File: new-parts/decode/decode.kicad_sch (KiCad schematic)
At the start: 37 parts, among them J1 BHR-10-VUA, J10 Conn_02x01, J11 Conn_02x01, J12 Conn_02x01, J13 Conn_02x01, J14 Conn_02x01, J2 Conn_02x01, J3 Conn_02x01, J4 Conn_02x01, J5 Conn_02x01, J6 Conn_02x03_Odd_Even, J7 Conn_02x01, J8 Conn_02x01, J9 Conn_02x01, K1 J104D2C12VDC.15S, K2 J104D2C12VDC.15S, K3 J104D2C12VDC.15S, K4 J104D2C12VDC.15S, K5 J104D2C12VDC.15S, K6 J104D2C12VDC.15S, K7 J104D2C12VDC.15S, K8 J104D2C12VDC.15S, K9 J104D2C12VDC.15S

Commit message: Layout decoder.
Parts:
- added TP2, TP3, TP4, TP5, TP6, TP7, TP8: TestPoint, TestPoint:TestPoint_Pad_D1.5mm, symbol Connector:TestPoint
- renumbered K4 to K3, K3 to K4
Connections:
- net GND: now also K9.22; no longer K9.12
- net VCC: now also K9.24; no longer K9.14
- net a en: now also K1.24, TP6.1; no longer K1.14
- net a en out: now also J4.1 (Pin_1), K1.21; no longer J3.1 (Pin_1), K1.11
- net add: now also TP3.1
- net c2: now also TP4.1
- net cf: now also K9.21; no longer K9.11
- net cinv: now also TP5.1
- net cond: now also TP2.1
- net m en: now also TP8.1
- net p en: now also K1.14, TP7.1; no longer K1.24
- net p en out: now also J3.1 (Pin_1), K1.11; no longer J4.1 (Pin_1), K1.21
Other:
- note added: "operand source out"
- note removed: "result source out"
- moved on the sheet: J10, J11, J12, J13, J14, J2, J6, J7, J8, J9

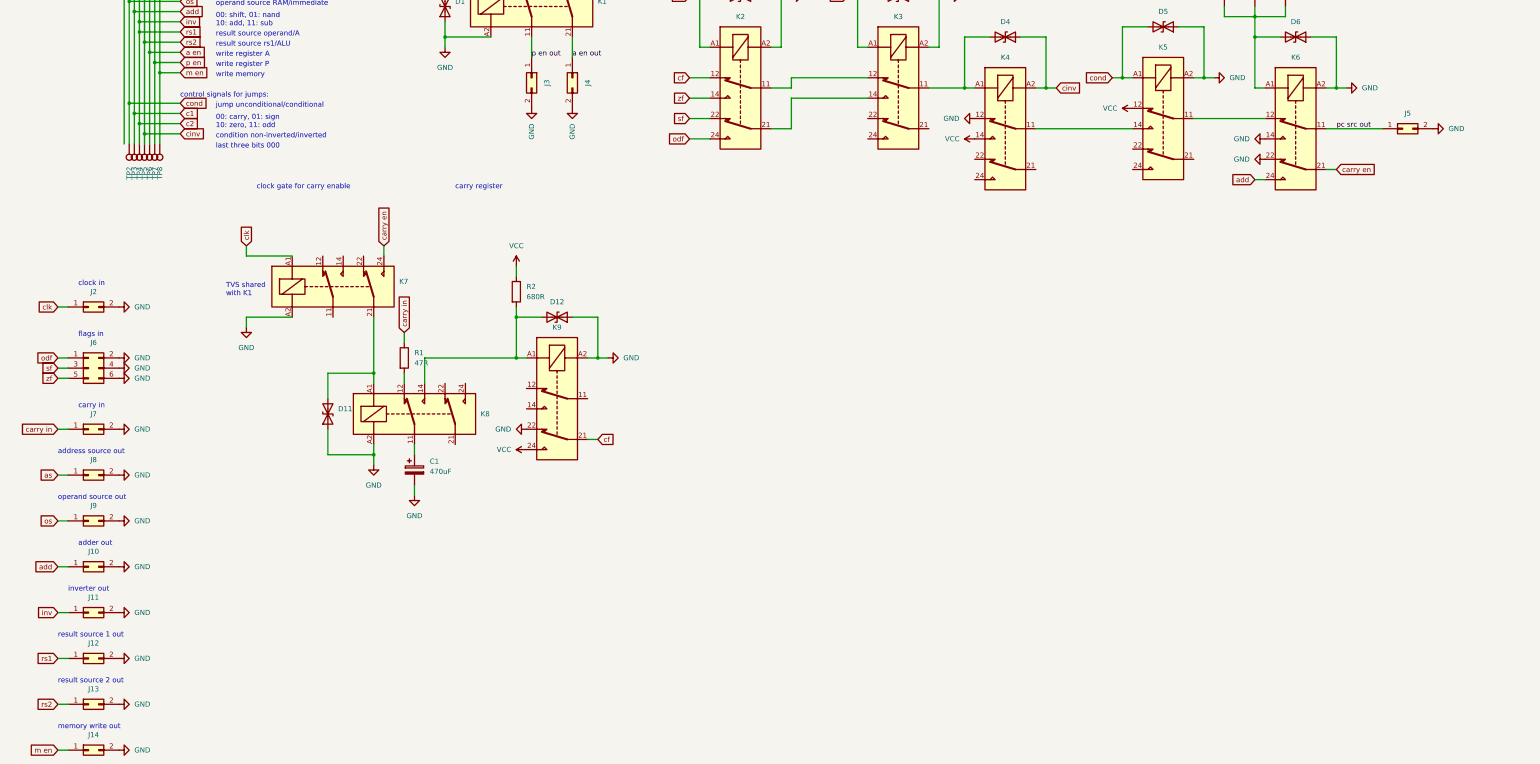
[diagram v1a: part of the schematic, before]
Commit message: Change all two-pin headers for control + ground to control only.
This is to prevent accidental short circuits when they are plugged in the
wrong way.
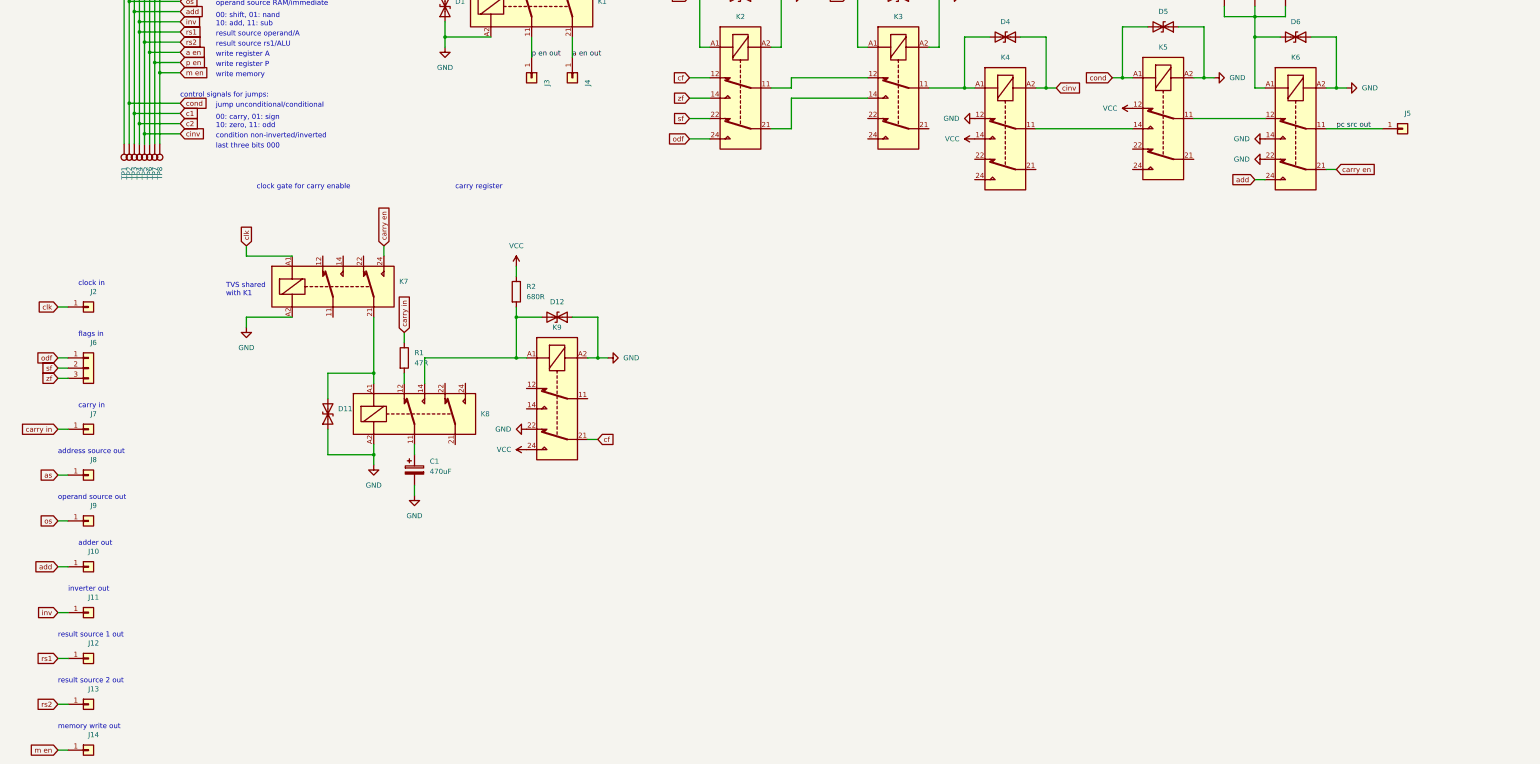
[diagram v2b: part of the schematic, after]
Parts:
- added TP1: TestPoint, TestPoint:TestPoint_Pad_D1.5mm, symbol Connector:TestPoint
- J10, J11, J12, J13, J14, J2, J3, J4, J5, J7, J8, J9: footprint Connector_PinHeader_2.54mm:PinHeader_1x02_P2.54mm_Vertical -> Connector_PinHeader_2.54mm:PinHeader_1x01_P2.54mm_Vertical; symbol Connector_Generic:Conn_02x01 -> Connector_Generic:Conn_01x01
- J6: footprint Connector_PinHeader_2.54mm:PinHeader_2x03_P2.54mm_Vertical -> Connector_PinHeader_2.54mm:PinHeader_1x03_P2.54mm_Vertical; symbol Connector_Generic:Conn_02x03_Odd_Even -> Connector_Generic:Conn_01x03
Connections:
- net GND: no longer J10.2 (Pin_2), J11.2 (Pin_2), J12.2 (Pin_2), J13.2 (Pin_2), J14.2 (Pin_2), J2.2 (Pin_2), J3.2 (Pin_2), J4.2 (Pin_2), J5.2 (Pin_2), J6.2 (Pin_2), J6.4 (Pin_4), J6.6 (Pin_6), J7.2 (Pin_2), J8.2 (Pin_2), J9.2 (Pin_2)
- net as: now also TP1.1
- net sf: now also J6.2 (Pin_2); no longer J6.3 (Pin_3)
- net zf: now also J6.3 (Pin_3); no longer J6.5 (Pin_5)

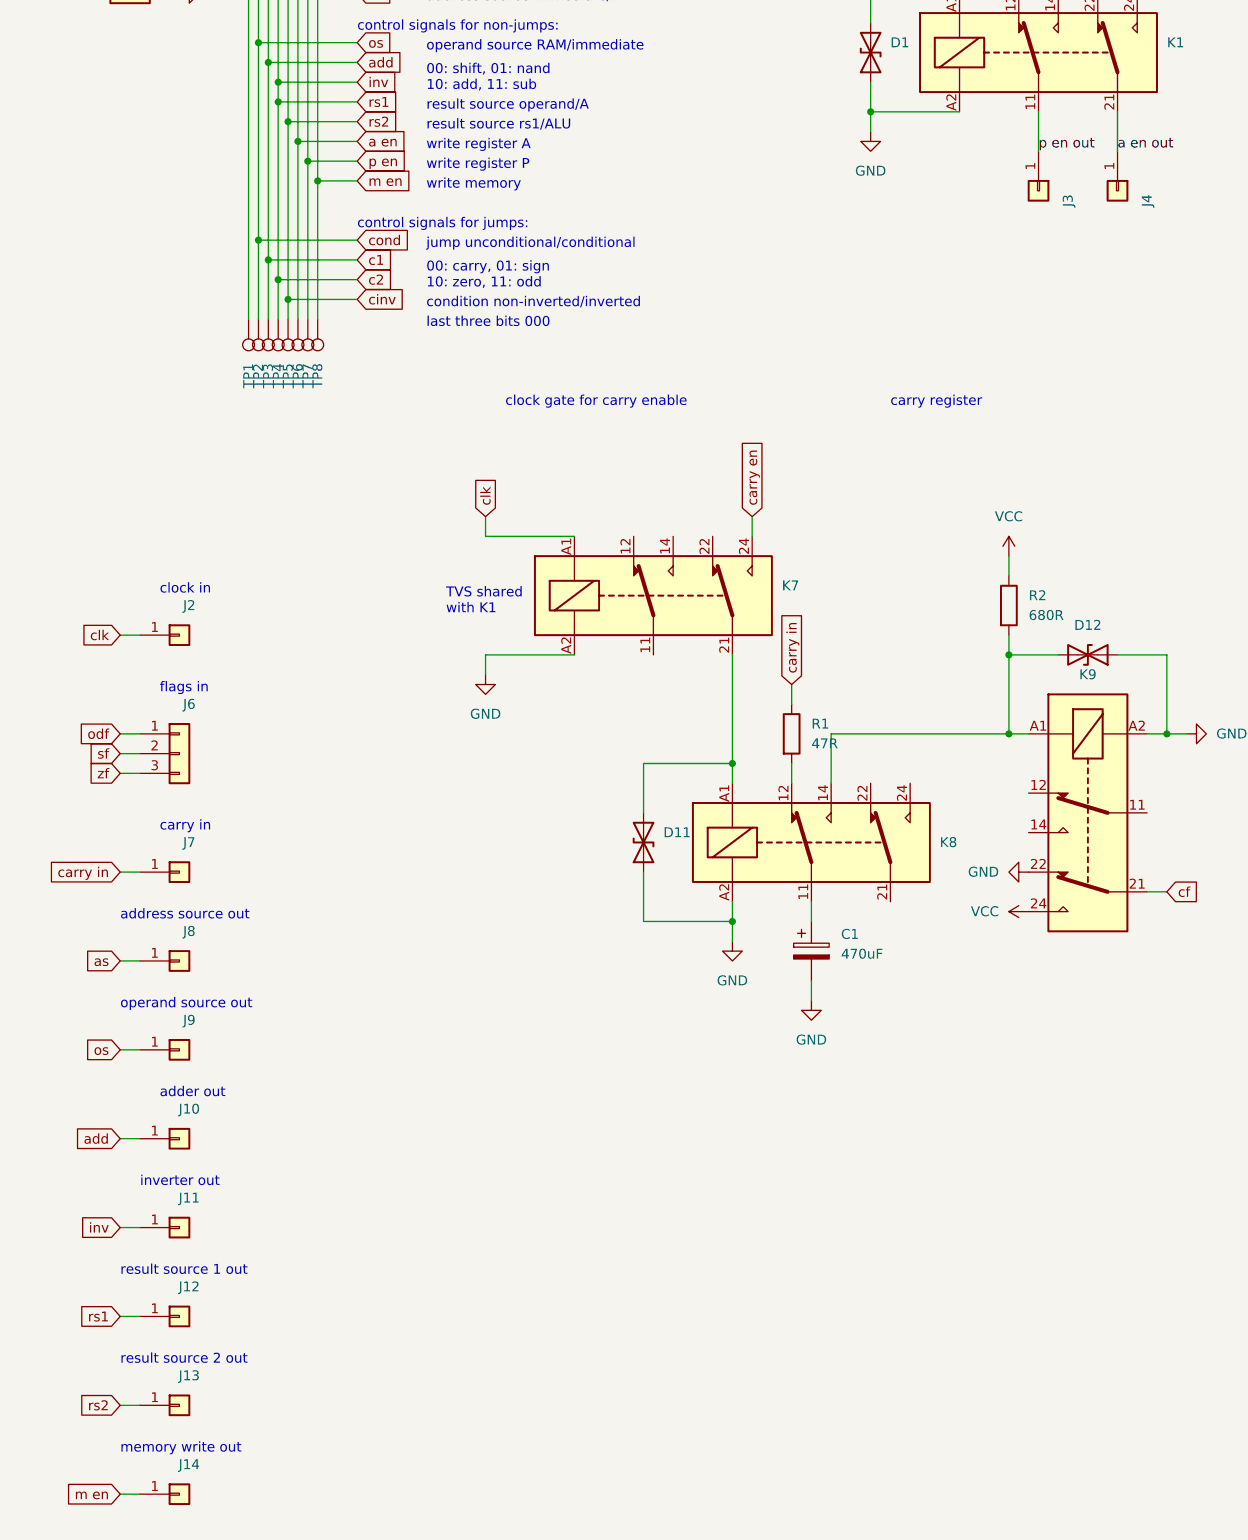
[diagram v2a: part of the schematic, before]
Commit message: Fix connector values: change names from 2 rows to 1 row.
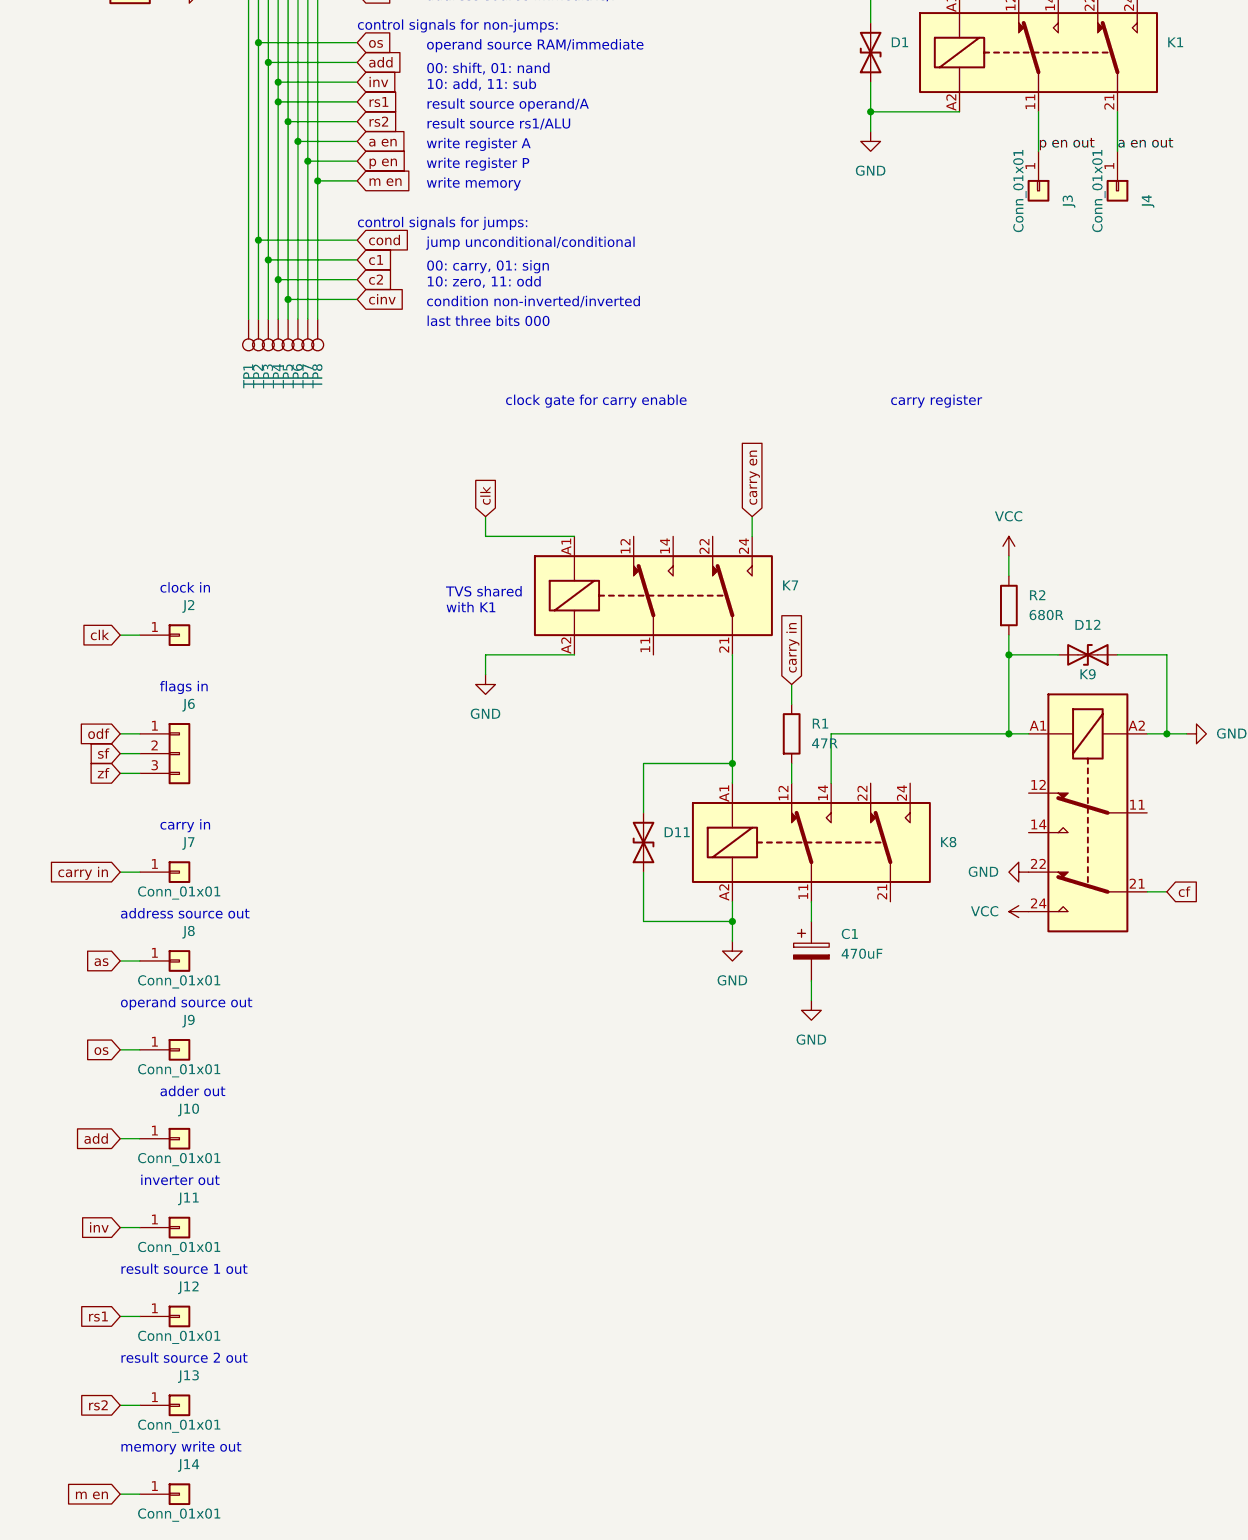
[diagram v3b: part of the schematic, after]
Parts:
- J10, J11, J12, J13, J14, J2, J3, J4, J5, J7, J8, J9: value Conn_02x01 -> Conn_01x01
- J6: value Conn_02x03_Odd_Even -> Conn_01x03
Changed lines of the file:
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@@
       (effects (font (size 1.27 1.27)))
     )
-    (property "Value" "Conn_02x01" (at 35.56 152.4 0)
-      (effects (font (size 1.27 1.27)) hide)
+    (property "Value" "Conn_01x01" (at 34.29 158.75 0)
+      (effects (font (size 1.27 1.27)))
     )
     (property "Footprint" "Connector_PinHeader_2.54mm:PinHeader_1x01_P2.54mm_Vertical" (at 34.29 156.21 0)
@@
       (effects (font (size 1.27 1.27)))
     )
-    (property "Value" "Conn_02x01" (at 158.75 58.42 0)
-      (effects (font (size 1.27 1.27)) hide)
+    (property "Value" "Conn_01x01" (at 152.4 57.15 0)
+      (effects (font (size 1.27 1.27)))
     )
     (property "Footprint" "Connector_PinHeader_2.54mm:PinHeader_1x01_P2.54mm_Vertical" (at 154.94 57.15 0)
@@
       (effects (font (size 1.27 1.27)))
     )
-    (property "Value" "Conn_02x01" (at 35.56 198.12 0)
-      (effects (font (size 1.27 1.27)) hide)
+    (property "Value" "Conn_01x01" (at 34.29 204.47 0)
+      (effects (font (size 1.27 1.27)))
     )
     (property "Footprint" "Connector_PinHeader_2.54mm:PinHeader_1x01_P2.54mm_Vertical" (at 34.29 201.93 0)
@@
       (effects (font (size 1.27 1.27)))
     )
-    (property "Value" "Conn_02x01" (at 35.56 220.98 0)
-      (effects (font (size 1.27 1.27)) hide)
+    (property "Value" "Conn_01x01" (at 34.29 227.33 0)
+      (effects (font (size 1.27 1.27)))
     )
     (property "Footprint" "Connector_PinHeader_2.54mm:PinHeader_1x01_P2.54mm_Vertical" (at 34.29 224.79 0)
@@
       (effects (font (size 1.27 1.27)))
     )
-    (property "Value" "Conn_02x01" (at 35.56 186.69 0)
-      (effects (font (size 1.27 1.27)) hide)
+    (property "Value" "Conn_01x01" (at 34.29 193.04 0)
+      (effects (font (size 1.27 1.27)))
     )
     (property "Footprint" "Connector_PinHeader_2.54mm:PinHeader_1x01_P2.54mm_Vertical" (at 34.29 190.5 0)
@@
       (effects (font (size 1.27 1.27)))
     )
-    (property "Value" "Conn_02x01" (at 35.56 163.83 0)
-      (effects (font (size 1.27 1.27)) hide)
+    (property "Value" "Conn_01x01" (at 34.29 170.18 0)
+      (effects (font (size 1.27 1.27)))
     )
     (property "Footprint" "Connector_PinHeader_2.54mm:PinHeader_1x01_P2.54mm_Vertical" (at 34.29 167.64 0)
@@
       (effects (font (size 1.27 1.27)))
     )
-    (property "Value" "Conn_02x01" (at 148.59 58.42 0)
-      (effects (font (size 1.27 1.27)) hide)
+    (property "Value" "Conn_01x01" (at 142.24 57.15 0)
+      (effects (font (size 1.27 1.27)))
     )
     (property "Footprint" "Connector_PinHeader_2.54mm:PinHeader_1x01_P2.54mm_Vertical" (at 144.78 57.15 0)
@@
       (effects (font (size 1.27 1.27)))
     )
-    (property "Value" "Conn_02x03_Odd_Even" (at 35.56 123.19 0)
+    (property "Value" "Conn_01x03" (at 35.56 123.19 0)
       (effects (font (size 1.27 1.27)) hide)
     )
@@
       (effects (font (size 1.27 1.27)))
     )
-    (property "Value" "Conn_02x01" (at 35.56 110.49 0)
+    (property "Value" "Conn_01x01" (at 35.56 110.49 0)
       (effects (font (size 1.27 1.27)) hide)
     )
@@
       (effects (font (size 1.27 1.27)))
     )
-    (property "Value" "Conn_02x01" (at 363.22 66.04 0)
+    (property "Value" "Conn_01x01" (at 363.22 66.04 0)
       (effects (font (size 1.27 1.27)) hide)
     )
@@
       (effects (font (size 1.27 1.27)))
     )
-    (property "Value" "Conn_02x01" (at 35.56 140.97 0)
-      (effects (font (size 1.27 1.27)) hide)
+    (property "Value" "Conn_01x01" (at 34.29 147.32 0)
+      (effects (font (size 1.27 1.27)))
     )
     (property "Footprint" "Connector_PinHeader_2.54mm:PinHeader_1x01_P2.54mm_Vertical" (at 34.29 144.78 0)
@@
       (effects (font (size 1.27 1.27)))
     )
-    (property "Value" "Conn_02x01" (at 35.56 175.26 0)
-      (effects (font (size 1.27 1.27)) hide)
+    (property "Value" "Conn_01x01" (at 34.29 181.61 0)
+      (effects (font (size 1.27 1.27)))
     )
     (property "Footprint" "Connector_PinHeader_2.54mm:PinHeader_1x01_P2.54mm_Vertical" (at 34.29 179.07 0)
@@
       (effects (font (size 1.27 1.27)))
     )
-    (property "Value" "Conn_02x01" (at 35.56 209.55 0)
-      (effects (font (size 1.27 1.27)) hide)
+    (property "Value" "Conn_01x01" (at 34.29 215.9 0)
+      (effects (font (size 1.27 1.27)))
     )
     (property "Footprint" "Connector_PinHeader_2.54mm:PinHeader_1x01_P2.54mm_Vertical" (at 34.29 213.36 0)
